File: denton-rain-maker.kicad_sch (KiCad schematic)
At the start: 70 parts, among them J1 Live(AC2), J2 Neutral(AC1), J3 SEED C3, Q1 BT136S-800E, Q2 BT136S-800E, Q3 BT136S-800E, Q4 BT136S-800E, SW1 SW_Rotary_1x8_MP, U1 MOC3063M, U2 MOC3063M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

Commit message: rotary switch checkpoint
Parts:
- added D10: LED, symbol Device:LED
- added R36: 10k, Resistor_SMD:R_1206_3216Metric_Pad1.30x1.75mm_HandSolder, symbol Device:R_Small_US
- added R37: 220, Resistor_SMD:R_1206_3216Metric_Pad1.30x1.75mm_HandSolder, symbol Device:R_Small_US
- C1, C11: footprint (none) -> Capacitor_SMD:C_1206_3216Metric_Pad1.33x1.80mm_HandSolder
- C12: footprint (none) -> Capacitor_THT:CP_Radial_D10.0mm_P5.00mm
- C3: footprint (none) -> Capacitor_THT:CP_Radial_D6.3mm_P2.50mm
- J1, J2: footprint (none) -> Connector_PinSocket_1.27mm:PinSocket_1x01_P1.27mm_Vertical
- J3: footprint Module:XIAO-ESP32C3-SMD_alex -> Symbol:XIAO-ESP32C3-SMD_alex
- R5: value 22.6k -> 30k
- R6, R7, R8: footprint (none) -> Resistor_SMD:R_1206_3216Metric_Pad1.30x1.75mm_HandSolder
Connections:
- net GND: now also D10.1 (K), R36.1; no longer R19.1
- net at J3.2 (Pin_8), R13.2, R14.1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: now also R13.1, R14.2, R19.1, SW1.3, R36.2
- net at C10.1, C3.1, C8.1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: now also R37.2
- new net: D10.2 (A), R37.1

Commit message: starting on layout
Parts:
- removed D2, D5, D7: LED, LED_SMD:LED_1206_3216Metric_Pad1.42x1.75mm_HandSolder, symbol Device:LED
- removed D3, D4, D6: 1N4148W, Diode_SMD:D_SOD-123, symbol Diode:1N4148W
- removed J1: Live(AC2), Connector_PinSocket_1.27mm:PinSocket_1x01_P1.27mm_Vertical, symbol Connector:Conn_01x01_Socket
- removed J2: Neutral(AC1), Connector_PinSocket_1.27mm:PinSocket_1x01_P1.27mm_Vertical, symbol Connector:Conn_01x01_Socket
- removed Q1, Q2, Q3: BT136S-800E, Package_TO_SOT_SMD:TO-252-3_TabPin2, symbol Triac_Thyristor:BT136-800
- removed R1, R16, R17, R18, R19, R20, R9: 10k, Resistor_SMD:R_1206_3216Metric_Pad1.30x1.75mm_HandSolder, symbol Device:R_Small_US
- removed R10, R21, R4: 24V_Solenoid, symbol Device:R_Small_US
- removed R11, R12, R2, R22, R23, R3: 220, Resistor_SMD:R_1206_3216Metric_Pad1.30x1.75mm_HandSolder, symbol Device:R_Small_US
- removed SW1: SW_Rotary_1x8_MP, symbol Switch:SW_Rotary_1x8_MP
- removed U1, U2, U3: MOC3063M, Package_DIP:DIP-6_W7.62mm, symbol Relay_SolidState:MOC3063M
- added D11, D13, D15, D17: LED, LED_THT:LED_D3.0mm, symbol Device:LED
- added D12, D14, D16: 1N4148W, Diode_SMD:D_SOD-123, symbol Diode:1N4148W
- added J1: Conn_01x06, TerminalBlock_Phoenix:TerminalBlock_Phoenix_MPT-0,5-6-2.54_1x06_P2.54mm_Horizontal, symbol Connector_Generic:Conn_01x06
- added Q5, Q6, Q7: BT136S-800E, Package_TO_SOT_SMD:TO-252-3_TabPin2, symbol Triac_Thyristor:BT136-800
- added R38, R40, R42, R43: 220, Resistor_SMD:R_1206_3216Metric_Pad1.30x1.75mm_HandSolder, symbol Device:R_Small_US
- added R39, R44: 100, Resistor_SMD:R_1206_3216Metric_Pad1.30x1.75mm_HandSolder, symbol Device:R_Small_US
- added R41: 10k, Resistor_SMD:R_1206_3216Metric_Pad1.30x1.75mm_HandSolder, symbol Device:R_Small_US
- added S1: RDS7-8S-1065-73-D-67, Downloads:SW_RDS7-8S-1065-73-D-67, symbol RDS7-8S-1065-73-D-67:RDS7-8S-1065-73-D-67
- added U6, U7, U8: MOC3063M, Package_DIP:DIP-6_W7.62mm, symbol Relay_SolidState:MOC3063M
- D10: footprint (none) -> LED_THT:LED_D3.0mm
- D9: footprint LED_SMD:LED_1206_3216Metric_Pad1.42x1.75mm_HandSolder -> LED_THT:LED_D3.0mm
- R25: value 24V_Solenoid -> 10k; footprint (none) -> Resistor_SMD:R_1206_3216Metric_Pad1.30x1.75mm_HandSolder
- R28, R29, R30, R31, R36: value 10k -> 220
- R34: value 100 -> 220
- R35: value 100 -> 10k
- R5: value 30k -> 220
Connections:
- net GND: now also D11.1 (K), S1.C1 (C), S1.C2 (C__1), U6.2, U7.2, U8.2; no longer R36.1
- net at J3.20 (Pin_7): now also R30.2
- net at R31.1: now also U6.6
- net LINE_IN: now reaches D1.1, Q4.2 (A2), R27.2, R32.1, R33.1
- net LINE_IN: now also R31.2, J1.6 (Pin_6), Q5.2 (A2), Q6.2 (A2), Q7.2 (A2), R38.2, R39.1, R43.2, R44.1; no longer D8.1 (K), R25.1, R34.1, R35.1
- net at J3.7 (Pin_3): now also R42.2
- net at R28.1, U4.4: no longer Q4.3 (G)
- net NEUT: now reaches D8.2 (A), D9.1 (K)
- net NEUT: now also D1.2, D12.2 (A), D13.1 (K), D14.2 (A), D15.1 (K), D16.2 (A), D17.1 (K), J1.5 (Pin_5)
- net at R30.1: now also U6.1
- net at C6.1: now also R39.2; no longer R34.2
- net at R35.2: now also C6.2, D14.1 (K), J1.2 (Pin_2), Q6.1 (A1); no longer C7.1
- net at R29.1: now also U6.4
- net at J3.3.3V (Pin_3): now also R13.1, R14.1, R15.1; no longer R5.1
- net at J3.21 (Pin_2): now also R36.2
- net at J3.3 (Pin_7): now also R13.2, S1.2
- net at J3.4 (Pin_6): now also R15.2, S1.4
- net at J3.5 (Pin_5): now also R5.2
- new net: J3.2 (Pin_8), R14.2, S1.1
- new net: C7.1, R44.2
- new net: C7.2, D16.1 (K), J1.1 (Pin_1), Q7.1 (A1), R41.2
- new net: C5.2, D12.1 (K), J1.3 (Pin_3), Q5.1 (A1), R25.2
- new net: Q5.3 (G), R29.2
- new net: C4.2, D8.1 (K), J1.4 (Pin_4), Q4.1 (A1), R24.2
- new net: Q4.3 (G), R28.2
- new net: D17.2 (A), R41.1
- new net: R36.1, U7.1
- new net: R34.1, U7.4
- new net: R38.1, U7.6
- new net: Q6.3 (G), R34.2
- new net: D13.2 (A), R25.1
- new net: D15.2 (A), R35.1
- new net: R40.1, U8.4
- new net: Q7.3 (G), R40.2
- new net: R42.1, U8.1
- new net: R43.1, U8.6
- new net: D11.2 (A), R5.1
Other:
- moved on the sheet: C4, D8, D9, Q4, R24, R28, R32

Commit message: layout continues
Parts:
- L1: footprint (none) -> Inductor_SMD:L_Bourns_SRN6045TA
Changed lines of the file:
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@@
 			)
 		)
-		(property "Footprint" ""
+		(property "Footprint" "Inductor_SMD:L_Bourns_SRN6045TA"
 			(at 186.69 45.72 0)
 			(hide yes)

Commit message: gotta stop
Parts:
- removed C10: 47uF, symbol Device:C_Small_US
- C8, C9: footprint (none) -> Capacitor_SMD:C_1206_3216Metric_Pad1.33x1.80mm_HandSolder
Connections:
- net at R14.2, S1.1: now also J3.3 (Pin_7); no longer J3.2 (Pin_8)
- net at R13.2, S1.2: now also J3.4 (Pin_6); no longer J3.3 (Pin_7)
- net at R15.2, S1.4: now also J3.2 (Pin_8); no longer J3.4 (Pin_6)
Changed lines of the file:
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@@
 	)
 	(junction
-		(at 81.28 33.02)
-		(diameter 0)
-		(color 0 0 0 0)
-	)
-	(junction
 		(at 27.94 41.91)
 		(diameter 0)
@@
 	)
 	(junction
-		(at 129.54 38.1)
-		(diameter 0)
-		(color 0 0 0 0)
-	)
-	(junction
 		(at 173.99 137.16)
 		(diameter 0)
@@
 	)
 	(junction
-		(at 135.89 33.02)
-		(diameter 0)
-		(color 0 0 0 0)
-	)
-	(junction
 		(at 115.57 119.38)
 		(diameter 0)
@@
 	)
 	(junction
+		(at 81.28 33.02)
+		(diameter 0)
+		(color 0 0 0 0)
+	)
+	(junction
 		(at 81.28 24.13)
 		(diameter 0)
@@
 	(wire
 		(pts
+			(xy 78.74 34.29) (xy 85.09 34.29)
+		)
+		(stroke
+			(width 0)
+			(type default)
+		)
+	)
+	(wire
+		(pts
 			(xy 93.98 154.94) (xy 101.6 154.94)
 		)
@@
 	(wire
 		(pts
-			(xy 120.65 33.02) (xy 135.89 33.02)
+			(xy 120.65 33.02) (xy 142.24 33.02)
 		)
 		(stroke
@@
 	(wire
 		(pts
-			(xy 71.12 154.94) (xy 93.98 154.94)
+			(xy 76.2 39.37) (xy 76.2 38.1)
 		)
 		(stroke
@@
 	(wire
 		(pts
-			(xy 120.65 33.02) (xy 115.57 33.02)
+			(xy 71.12 154.94) (xy 93.98 154.94)
 		)
 		(stroke
@@
 	(wire
 		(pts
-			(xy 181.61 86.36) (xy 181.61 119.38)
+			(xy 120.65 33.02) (xy 115.57 33.02)
 		)
 		(stroke
@@
 	(wire
 		(pts
-			(xy 231.14 60.96) (xy 240.03 60.96)
+			(xy 181.61 86.36) (xy 181.61 119.38)
 		)
 		(stroke
@@
 	(wire
 		(pts
-			(xy 81.28 40.64) (xy 81.28 44.45)
+			(xy 231.14 60.96) (xy 240.03 60.96)
 		)
 		(stroke
@@
 	(wire
 		(pts
-			(xy 62.23 154.94) (xy 62.23 137.16)
+			(xy 81.28 40.64) (xy 81.28 44.45)
 		)
 		(stroke
@@
 	(wire
 		(pts
-			(xy 142.24 45.72) (xy 142.24 33.02)
+			(xy 62.23 154.94) (xy 62.23 137.16)
 		)
 		(stroke
@@
 	(wire
 		(pts
-			(xy 76.2 35.56) (xy 76.2 39.37)
+			(xy 142.24 45.72) (xy 142.24 33.02)
 		)
 		(stroke
@@
 	(wire
 		(pts
-			(xy 142.24 33.02) (xy 135.89 33.02)
-		)
-		(stroke
-			(width 0)
-			(type default)
-		)
-	)
-	(wire
-		(pts
 			(xy 74.93 33.02) (xy 81.28 33.02)
 		)
@@
 	(wire
 		(pts
-			(xy 81.28 33.02) (xy 92.71 33.02)
-		)
-		(stroke
-			(width 0)
-			(type default)
-		)
-	)
-	(wire
-		(pts
 			(xy 165.1 99.06) (xy 170.18 99.06)
 		)
@@
 	(wire
 		(pts
-			(xy 120.65 38.1) (xy 129.54 38.1)
+			(xy 83.82 119.38) (xy 83.82 123.19)
 		)
 		(stroke
@@
 	(wire
 		(pts
-			(xy 83.82 119.38) (xy 83.82 123.19)
+			(xy 85.09 33.02) (xy 92.71 33.02)
 		)
 		(stroke
@@
 	(wire
 		(pts
-			(xy 115.57 38.1) (xy 120.65 38.1)
+			(xy 85.09 34.29) (xy 85.09 33.02)
 		)
 		(stroke
@@
 	(wire
 		(pts
-			(xy 102.87 45.72) (xy 130.81 45.72)
+			(xy 115.57 38.1) (xy 120.65 38.1)
 		)
 		(stroke
@@
 	(wire
 		(pts
-			(xy 63.5 24.13) (xy 72.39 24.13)
+			(xy 102.87 45.72) (xy 130.81 45.72)
 		)
 		(stroke
@@
 	(wire
 		(pts
-			(xy 78.74 41.91) (xy 78.74 38.1)
+			(xy 63.5 24.13) (xy 72.39 24.13)
 		)
 		(stroke
@@
 	(wire
 		(pts
-			(xy 58.42 36.83) (xy 74.93 36.83)
+			(xy 78.74 34.29) (xy 78.74 41.91)
 		)
 		(stroke
@@
 	(wire
 		(pts
-			(xy 157.48 124.46) (xy 148.59 124.46)
+			(xy 58.42 36.83) (xy 74.93 36.83)
 		)
 		(stroke
@@
 	(wire
 		(pts
-			(xy 275.59 63.5) (xy 261.62 63.5)
+			(xy 157.48 124.46) (xy 148.59 124.46)
 		)
 		(stroke
@@
 	(wire
 		(pts
-			(xy 231.14 67.31) (xy 240.03 67.31)
+			(xy 275.59 63.5) (xy 261.62 63.5)
 		)
 		(stroke
@@
 	(wire
 		(pts
-			(xy 78.74 38.1) (xy 92.71 38.1)
+			(xy 231.14 67.31) (xy 240.03 67.31)
 		)
 		(stroke
@@
 	(wire
 		(pts
-			(xy 129.54 38.1) (xy 135.89 38.1)
-		)
-		(stroke
-			(width 0)
-			(type default)
-		)
-	)
-	(wire
-		(pts
 			(xy 170.18 132.08) (xy 177.8 132.08)
 		)
@@
 	(wire
 		(pts
+			(xy 81.28 33.02) (xy 81.28 35.56)
+		)
+		(stroke
+			(width 0)
+			(type default)
+		)
+	)
+	(wire
+		(pts
 			(xy 49.53 54.61) (xy 49.53 57.15)
 		)
@@
 	(wire
 		(pts
-			(xy 129.54 38.1) (xy 129.54 39.37)
+			(xy 120.65 38.1) (xy 120.65 39.37)
 		)
 		(stroke
@@
 	(wire
 		(pts
+			(xy 81.28 35.56) (xy 92.71 35.56)
+		)
+		(stroke
+			(width 0)
+			(type default)
+		)
+	)
+	(wire
+		(pts
 			(xy 250.19 48.26) (xy 261.62 48.26)
 		)
@@
 	(wire
 		(pts
-			(xy 92.71 35.56) (xy 76.2 35.56)
-		)
-		(stroke
-			(width 0)
-			(type default)
-		)
-	)
-	(wire
-		(pts
 			(xy 184.15 58.42) (xy 184.15 66.04)
 		)
@@
 		)
 	)
+	(wire
+		(pts
+			(xy 76.2 38.1) (xy 92.71 38.1)
+		)
+		(stroke
+			(width 0)
+			(type default)
+		)
+	)
 	(label ""
 		(at 195.58 162.56 0)
@@
 			)
 		)
-		(property "Footprint" ""
+		(property "Footprint" "Capacitor_SMD:C_1206_3216Metric_Pad1.33x1.80mm_HandSolder"
 			(at 115.57 35.56 0)
 			(hide yes)
@@
 	(symbol
 		(lib_id "power:GND")
-		(at 129.54 39.37 0)
+		(at 120.65 39.37 0)
 		(mirror y)
 		(unit 1)
@@
 		(fields_autoplaced yes)
 		(property "Reference" "#PWR09"
-			(at 129.54 45.72 0)
+			(at 120.65 45.72 0)
 			(hide yes)
 			(show_name no)
@@
 		)
 		(property "Value" "GND"
-			(at 129.54 44.45 0)
+			(at 120.65 44.45 0)
 			(hide yes)
 			(show_name no)
@@
 		)
 		(property "Footprint" ""
-			(at 129.54 39.37 0)
+			(at 120.65 39.37 0)
 			(hide yes)
 			(show_name no)
@@
 		)
 		(property "Datasheet" ""
-			(at 129.54 39.37 0)
+			(at 120.65 39.37 0)
 			(hide yes)
 			(show_name no)
@@
 		)
 		(property "Description" "Power symbol creates a global label with name \"GND\" , ground"
-			(at 129.54 39.37 0)
+			(at 120.65 39.37 0)
 			(hide yes)
 			(show_name no)
@@
 	)
 	(symbol
-		(lib_id "Device:C_Small_US")
-		(at 135.89 35.56 0)
-		(mirror y)
-		(unit 1)
-		(body_style 1)
-		(exclude_from_sim no)
-		(in_bom yes)
-		(on_board yes)
-		(in_pos_files yes)
-		(dnp no)
-		(fields_autoplaced yes)
-		(property "Reference" "C10"
-			(at 133.35 34.4169 0)
-			(show_name no)
-			(do_not_autoplace no)
-			(effects
-				(font
-					(size 1.27 1.27)
-				)
-				(justify left)
-			)
-		)
-		(property "Value" "47uF"
-			(at 133.35 36.9569 0)
-			(show_name no)
-			(do_not_autoplace no)
-			(effects
-				(font
-					(size 1.27 1.27)
-				)
-				(justify left)
-			)
-		)
-		(property "Footprint" ""
-			(at 135.89 35.56 0)
-			(hide yes)
-			(show_name no)
-			(do_not_autoplace no)
-			(effects
-				(font
-					(size 1.27 1.27)
-				)
-			)
-		)
-		(property "Datasheet" ""
-			(at 135.89 35.56 0)
-			(hide yes)
-			(show_name no)
-			(do_not_autoplace no)
-			(effects
-				(font
-					(size 1.27 1.27)
-				)
-			)
-		)
-		(property "Description" "capacitor, small US symbol"
-			(at 135.89 35.56 0)
-			(hide yes)
-			(show_name no)
-			(do_not_autoplace no)
-			(effects
-				(font
-					(size 1.27 1.27)
-				)
-			)
-		)
-		(pin "2"
-		)
-		(pin "1"
-		)
-		(instances
-			(project "denton-rain-maker"
-				(path "/63428df5-db84-42ba-8e0d-8c79f5e81619"
-					(reference "C10")
-					(unit 1)
-				)
-			)
-		)
-	)
-	(symbol
 		(lib_id "Device:R_Small_US")
 		(at 175.26 116.84 0)
@@
 			)
 		)
-		(property "Footprint" ""
+		(property "Footprint" "Capacitor_SMD:C_1206_3216Metric_Pad1.33x1.80mm_HandSolder"
 			(at 120.65 35.56 0)
 			(hide yes)

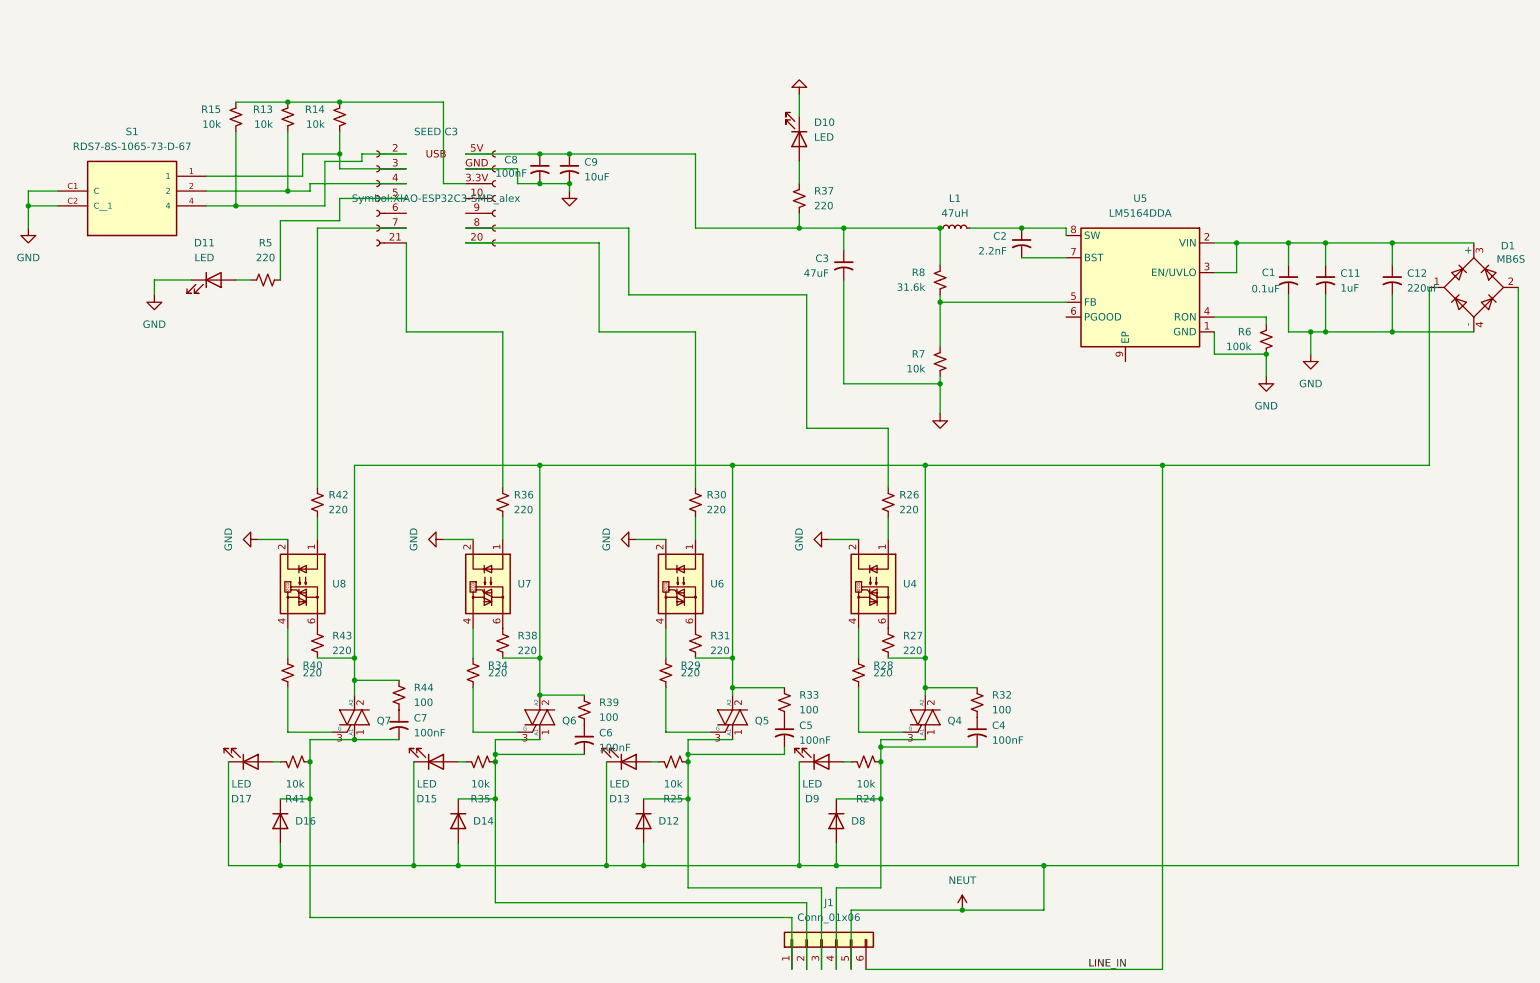
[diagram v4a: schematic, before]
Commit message: remember to change the buck converter
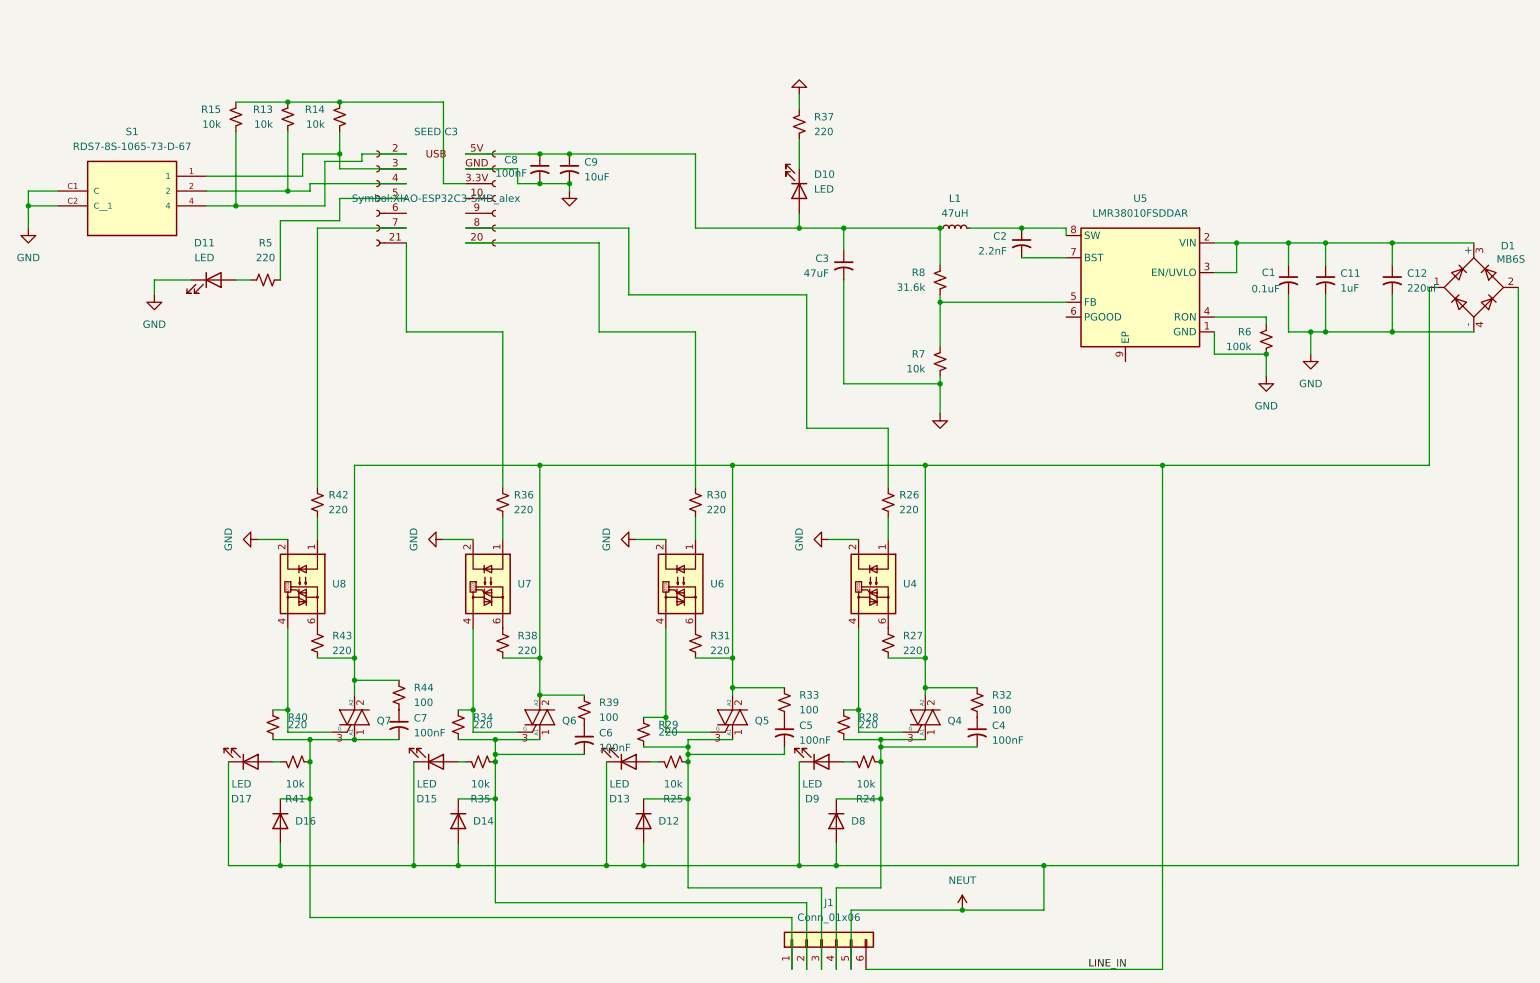
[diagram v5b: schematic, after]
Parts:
- U5: value LM5164DDA -> LMR38010FSDDAR; footprint Package_SO:HSOP-8-1EP_3.9x4.9mm_P1.27mm_EP2.41x3.1mm_ThermalVias -> Package_SO:Texas_R-PDSO-G8_EP2.95x4.9mm_Mask2.4x3.1mm
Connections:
- net GND: now also R37.1; no longer D10.1 (K)
- net at C6.2, D14.1 (K), J1.2 (Pin_2)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: now also R34.2
- net at C7.2, D16.1 (K), J1.1 (Pin_1)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: now also R40.2
- net at D10.2 (A): now also C3.1, C8.1, C9.1, J3.5V (Pin_1), L1.2, R8.1; no longer R37.1
- net at C5.2, D12.1 (K), J1.3 (Pin_3)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: now also R29.2
- net at Q5.3 (G): now also R29.1, U6.4; no longer R29.2
- net at C4.2, D8.1 (K), J1.4 (Pin_4)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: now also R28.2
- net at Q4.3 (G): now also R28.1, U4.4; no longer R28.2
- net at R34.1, U7.4: now also Q6.3 (G)
- net at R40.1, U8.4: now also Q7.3 (G)
- new net: D10.1 (K), R37.2
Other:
- moved on the sheet: D10, R28, R29, R34, R37, R40
